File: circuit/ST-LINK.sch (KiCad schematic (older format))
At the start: 2 parts, among them P2 CONN_01X06

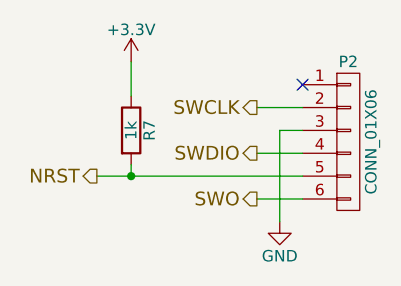
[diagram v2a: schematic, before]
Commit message: Servoのchを4->6に変更
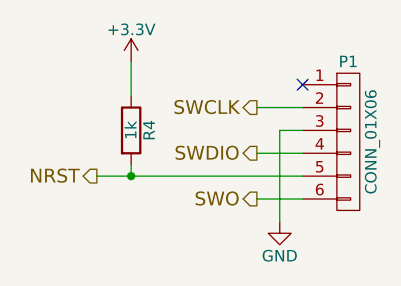
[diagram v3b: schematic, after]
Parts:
- renumbered P2 to P1, R7 to R4
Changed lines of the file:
@@
 LIBS:contrib
 LIBS:valves
+LIBS:stm32
 LIBS:robocon_sch
+LIBS:SamacSys_Parts
 LIBS:YASU
-LIBS:stm32
 LIBS:ServoDriver-cache
 EELAYER 25 0
@@
 $EndDescr
 $Comp
-L CONN_01X06 P2
+L CONN_01X06 P1
 U 1 1 58DA469F
 P 3800 2850
-F 0 "P2" H 3800 3200 50  0000 C CNN
+F 0 "P1" H 3800 3200 50  0000 C CNN
 F 1 "CONN_01X06" V 3900 2850 50  0000 C CNN
 F 2 "Pin_Headers:Pin_Header_Straight_1x06_Pitch2.54mm" H 3800 2850 50  0001 C CNN
@@
 	3600 3100 3400 3100
 $Comp
-L GND #PWR024
+L GND #PWR013
 U 1 1 58DA69EB
 P 3500 3200
-F 0 "#PWR024" H 3500 2950 50  0001 C CNN
+F 0 "#PWR013" H 3500 2950 50  0001 C CNN
 F 1 "GND" H 3500 3050 50  0000 C CNN
 F 2 "" H 3500 3200 50  0000 C CNN
@@
 SWO
 $Comp
-L R R7
+L R R4
 U 1 1 593DD523
 P 2850 2800
-F 0 "R7" V 2930 2800 50  0000 C CNN
+F 0 "R4" V 2930 2800 50  0000 C CNN
 F 1 "1k" V 2850 2800 50  0000 C CNN
 F 2 "Resistors_ThroughHole:R_Axial_DIN0207_L6.3mm_D2.5mm_P7.62mm_Horizontal" V 2780 2800 50  0001 C CNN
@@
 $EndComp
 $Comp
-L +3.3V #PWR025
+L +3.3V #PWR014
 U 1 1 593DD52A
 P 2850 2500
-F 0 "#PWR025" H 2850 2350 50  0001 C CNN
+F 0 "#PWR014" H 2850 2350 50  0001 C CNN
 F 1 "+3.3V" H 2850 2640 50  0000 C CNN
 F 2 "" H 2850 2500 50  0000 C CNN

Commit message: 回路図と部品表完了
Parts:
- R4: footprint Resistors_ThroughHole:R_Axial_DIN0207_L6.3mm_D2.5mm_P7.62mm_Horizontal -> Resistors_SMD:R_0603_HandSoldering
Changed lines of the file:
@@
 F 0 "R4" V 2930 2800 50  0000 C CNN
 F 1 "1k" V 2850 2800 50  0000 C CNN
-F 2 "Resistors_ThroughHole:R_Axial_DIN0207_L6.3mm_D2.5mm_P7.62mm_Horizontal" V 2780 2800 50  0001 C CNN
+F 2 "Resistors_SMD:R_0603_HandSoldering" V 2780 2800 50  0001 C CNN
 F 3 "" H 2850 2800 50  0000 C CNN
 	1    2850 2800

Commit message: チップ抵抗の大きさ変更とガーバー出力のための手直し
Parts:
- R4: footprint Resistors_SMD:R_0603_HandSoldering -> YASU:R_0603_HandSoldering_LP
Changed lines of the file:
@@
 F 0 "R4" V 2930 2800 50  0000 C CNN
 F 1 "1k" V 2850 2800 50  0000 C CNN
-F 2 "Resistors_SMD:R_0603_HandSoldering" V 2780 2800 50  0001 C CNN
+F 2 "YASU:R_0603_HandSoldering_LP" V 2780 2800 50  0001 C CNN
 F 3 "" H 2850 2800 50  0000 C CNN
 	1    2850 2800
